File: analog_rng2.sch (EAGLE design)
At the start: 63 parts, among them IC2 LM2903D, IC3 OPA4134D, U1 TLV73325, U2 TPS70925, U23423 LM277625

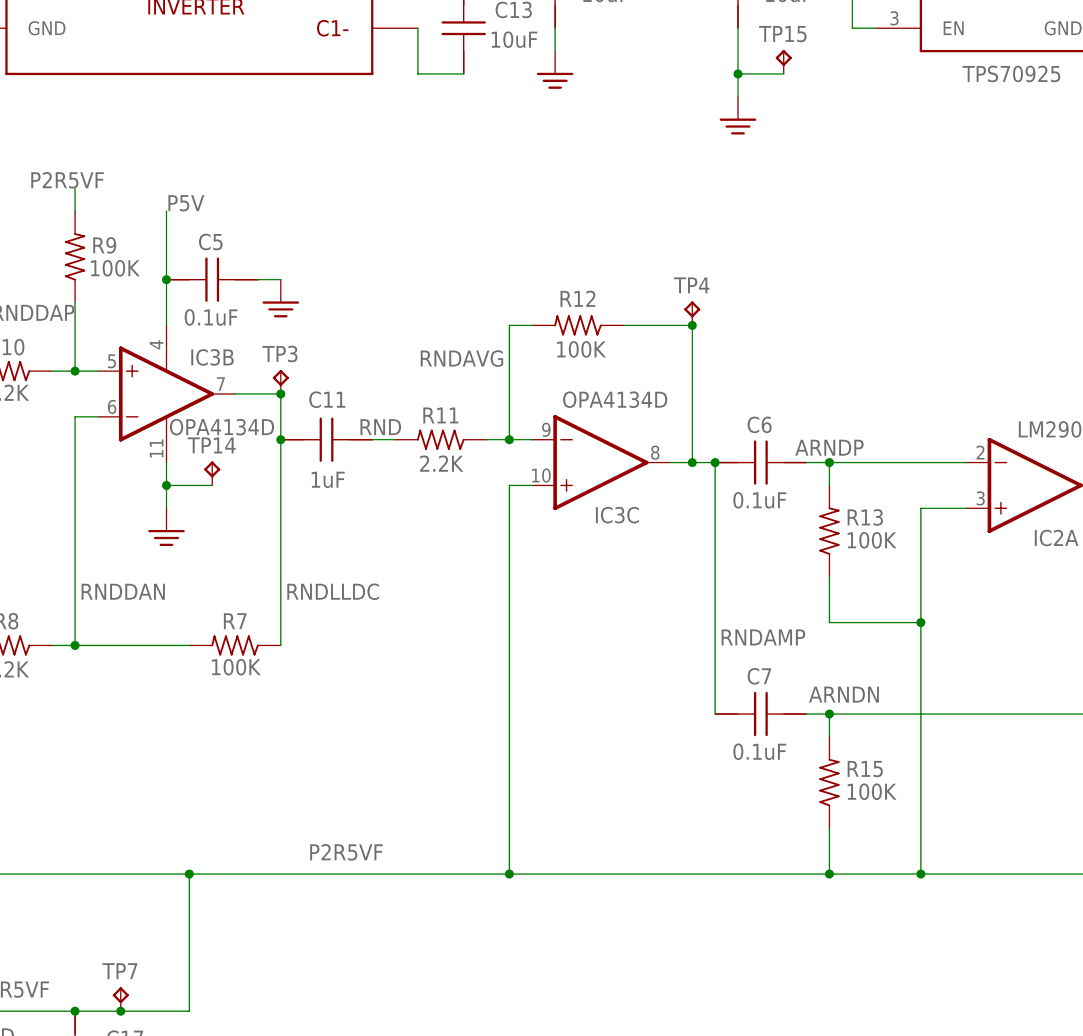
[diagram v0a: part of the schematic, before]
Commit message: More layout work done, finished first cut at copper layout
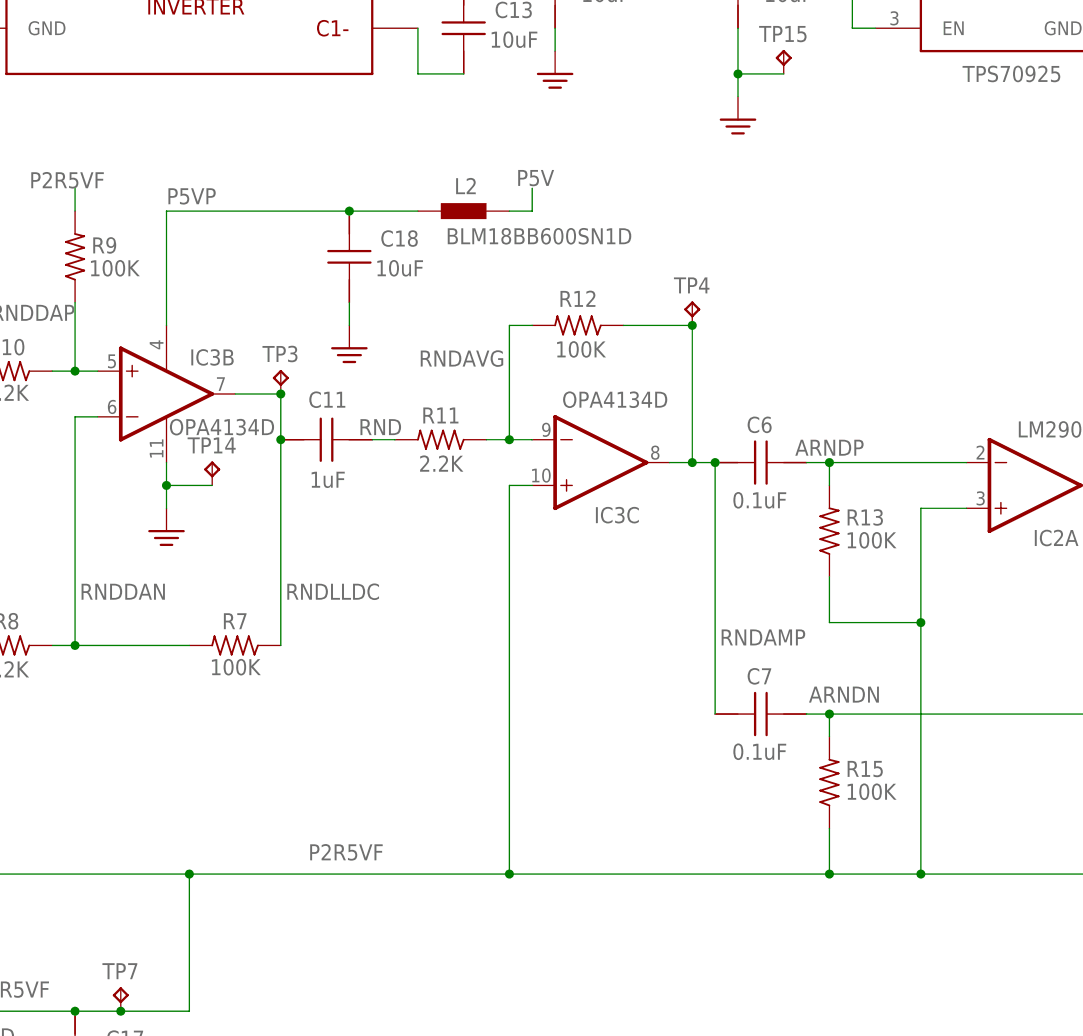
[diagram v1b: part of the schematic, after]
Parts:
- removed C5: 0.1uF, vreg_local:C-USC0603
- added C18: 10uF, vreg_local:C-USC1206
- added L2: BLM18BB600SN1D, vreg_local:BEADR0805
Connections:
- new net P5VP: C18.1, IC3P.V+, L2.1
- net P5V: now also L2.2; no longer C5.1, IC3P.V+
- net PE: now also C18.2; no longer C5.2
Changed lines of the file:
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@@
 <part name="FRAME1" library="frames" deviceset="FRAME_A_L" device=""/>
 <part name="R14" library="resistor" deviceset="R-US_" device="R1206" value="2.2K"/>
-<part name="SUPPLY11" library="supply2" deviceset="PE" device=""/>
 <part name="SUPPLY12" library="supply2" deviceset="PE" device=""/>
 <part name="SUPPLY13" library="supply2" deviceset="PE" device=""/>
@@
 <part name="SUPPLY5" library="supply2" deviceset="PE" device=""/>
 <part name="C10" library="vreg_local" deviceset="C-US" device="C0603" value="0.1uF"/>
-<part name="C5" library="vreg_local" deviceset="C-US" device="C0603" value="0.1uF"/>
 <part name="C6" library="vreg_local" deviceset="C-US" device="C0603" value="0.1uF"/>
 <part name="C7" library="vreg_local" deviceset="C-US" device="C0603" value="0.1uF"/>
@@
 <part name="TP17" library="testpad" deviceset="TP" device="PAD1-20"/>
 <part name="L1" library="vreg_local" deviceset="BEAD" device="R0805" value="BLM18BB600SN1D"/>
+<part name="C18" library="vreg_local" deviceset="C-US" device="C1206" value="10uF"/>
+<part name="L2" library="vreg_local" deviceset="BEAD" device="R0805" value="BLM18BB600SN1D"/>
+<part name="SUPPLY17" library="supply2" deviceset="PE" device=""/>
 </parts>
 <sheets>
@@
 <attribute name="VALUE" x="212.344" y="123.19" size="1.778" layer="96" align="center-left"/>
 </instance>
-<instance part="SUPPLY11" gate="PE" x="111.76" y="124.46" smashed="yes"/>
 <instance part="SUPPLY12" gate="PE" x="99.06" y="99.06" smashed="yes"/>
 <instance part="SUPPLY13" gate="PE" x="231.14" y="83.82" smashed="yes"/>
@@
 <attribute name="VALUE" x="221.996" y="158.369" size="1.778" layer="96"/>
 </instance>
-<instance part="C5" gate="G$1" x="104.14" y="127" smashed="yes" rot="R90">
-<attribute name="NAME" x="104.013" y="130.302" size="1.778" layer="95" align="bottom-center"/>
-<attribute name="VALUE" x="104.013" y="123.698" size="1.778" layer="96" align="top-center"/>
-</instance>
 <instance part="C6" gate="G$1" x="165.1" y="106.68" smashed="yes" rot="R90">
 <attribute name="NAME" x="164.973" y="109.982" size="1.778" layer="95" align="bottom-center"/>
@@
 <attribute name="VALUE" x="71.882" y="43.815" size="1.778" layer="96" align="top-center"/>
 </instance>
+<instance part="C18" gate="G$1" x="119.38" y="129.54" smashed="yes">
+<attribute name="NAME" x="124.968" y="130.683" size="1.778" layer="95" align="bottom-center"/>
+<attribute name="VALUE" x="124.968" y="129.159" size="1.778" layer="96" align="top-center"/>
+</instance>
+<instance part="L2" gate="G$1" x="132.08" y="134.62" smashed="yes">
+<attribute name="NAME" x="132.334" y="136.4996" size="1.778" layer="95" align="bottom-center"/>
+<attribute name="VALUE" x="140.462" y="132.715" size="1.778" layer="96" align="top-center"/>
+</instance>
+<instance part="SUPPLY17" gate="PE" x="119.38" y="119.38" smashed="yes"/>
 </instances>
 <busses>
@@
 <net name="PE" class="0">
 <segment>
-<pinref part="SUPPLY11" gate="PE" pin="PE"/>
-<wire x1="111.76" y1="127" x2="109.22" y2="127" width="0.1524" layer="91"/>
-<pinref part="C5" gate="G$1" pin="2"/>
-</segment>
-<segment>
 <pinref part="SUPPLY13" gate="PE" pin="PE"/>
 <wire x1="228.6" y1="88.9" x2="231.14" y2="88.9" width="0.1524" layer="91"/>
@@
 <wire x1="88.9" y1="33.02" x2="88.9" y2="35.56" width="0.1524" layer="91"/>
 <pinref part="SUPPLY16" gate="PE" pin="PE"/>
+</segment>
+<segment>
+<pinref part="SUPPLY17" gate="PE" pin="PE"/>
+<pinref part="C18" gate="G$1" pin="2"/>
+<wire x1="119.38" y1="121.92" x2="119.38" y2="124.46" width="0.1524" layer="91"/>
 </segment>
 </net>
@@
 </net>
 <net name="P2R5VF" class="0">
-<segment>
-<pinref part="R15" gate="G$1" pin="1"/>
-<wire x1="172.72" y1="60.96" x2="172.72" y2="66.04" width="0.1524" layer="91"/>
-<junction x="172.72" y="60.96"/>
-</segment>
 <segment>
 <wire x1="101.6" y1="45.72" x2="93.98" y2="45.72" width="0.1524" layer="91"/>
@@
 <junction x="35.56" y="60.96"/>
 <wire x1="101.6" y1="60.96" x2="137.16" y2="60.96" width="0.1524" layer="91"/>
-<wire x1="137.16" y1="60.96" x2="182.88" y2="60.96" width="0.1524" layer="91"/>
+<wire x1="137.16" y1="60.96" x2="172.72" y2="60.96" width="0.1524" layer="91"/>
+<wire x1="172.72" y1="60.96" x2="182.88" y2="60.96" width="0.1524" layer="91"/>
 <wire x1="208.28" y1="60.96" x2="182.88" y2="60.96" width="0.1524" layer="91"/>
 <pinref part="IC2" gate="B" pin="-IN"/>
@@
 <wire x1="101.6" y1="45.72" x2="101.6" y2="60.96" width="0.1524" layer="91"/>
 <junction x="101.6" y="60.96"/>
+<pinref part="R15" gate="G$1" pin="1"/>
+<wire x1="172.72" y1="66.04" x2="172.72" y2="60.96" width="0.1524" layer="91"/>
+<junction x="172.72" y="60.96"/>
 </segment>
 <segment>
@@
 </segment>
 <segment>
-<pinref part="C5" gate="G$1" pin="1"/>
-<wire x1="99.06" y1="121.92" x2="99.06" y2="127" width="0.1524" layer="91"/>
-<pinref part="IC3" gate="P" pin="V+"/>
-<wire x1="99.06" y1="127" x2="99.06" y2="134.62" width="0.1524" layer="91"/>
-<junction x="99.06" y="127"/>
-<label x="99.06" y="134.62" size="1.778" layer="95"/>
-</segment>
-<segment>
 <pinref part="U1" gate="G$1" pin="IN"/>
 <wire x1="10.16" y1="45.72" x2="5.08" y2="45.72" width="0.1524" layer="91"/>
@@
 <wire x1="5.08" y1="35.56" x2="5.08" y2="45.72" width="0.1524" layer="91"/>
 <label x="6.35" y="46.736" size="1.778" layer="95"/>
+</segment>
+<segment>
+<pinref part="L2" gate="G$1" pin="2"/>
+<wire x1="137.16" y1="134.62" x2="139.7" y2="134.62" width="0.1524" layer="91"/>
+<wire x1="139.7" y1="134.62" x2="139.7" y2="137.16" width="0.1524" layer="91"/>
+<label x="137.922" y="137.414" size="1.778" layer="95"/>
 </segment>
 </net>
@@
 </segment>
 </net>
+<net name="P5VP" class="0">
+<segment>
+<pinref part="L2" gate="G$1" pin="1"/>
+<pinref part="C18" gate="G$1" pin="1"/>
+<wire x1="127" y1="134.62" x2="119.38" y2="134.62" width="0.1524" layer="91"/>
+<wire x1="119.38" y1="134.62" x2="99.06" y2="134.62" width="0.1524" layer="91"/>
+<junction x="119.38" y="134.62"/>
+<wire x1="99.06" y1="134.62" x2="99.06" y2="121.92" width="0.1524" layer="91"/>
+<label x="99.06" y="135.382" size="1.778" layer="95"/>
+<pinref part="IC3" gate="P" pin="V+"/>
+</segment>
+</net>
